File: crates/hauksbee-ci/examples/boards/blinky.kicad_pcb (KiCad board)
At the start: 2 copper layers, 5 parts, among them U1 ATmega328P

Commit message: Add an MCP1702-3302 SOT-23A card and name the DIP-28 package in ATmega328P fixtures
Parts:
- U1: footprint Package_QFP:TQFP-32_7x7mm_P0.8mm -> Package_DIP:DIP-28_W7.62mm
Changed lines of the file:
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@@
-(kicad_pcb(version 20171130)(generator "pcbnew")(general(thickness 1.6))(paper "A4")(layers(0 "F.Cu"signal)(31 "B.Cu"signal)(36 "B.SilkS"user)(37 "F.SilkS"user)(38 "B.Mask"user)(39 "F.Mask"user)(44 "Edge.Cuts"user)(48 "B.Fab"user)(49 "F.Fab"user))(setup(pad_to_mask_clearance 0))(net 0 "")(net 1 "+5V")(net 2 "GND")(net 3 "D13")(net 4 "ADC0")(net 5 "LED_A")(footprint "Resistor_THT:R_Axial_DIN0207_L6.3mm_D2.5mm"(layer "F.Cu")(at -7.198 -6.605 0)(property "Reference""R2")(property "Value""10k")(pad 1 thru_hole circle(at 0 0 0)(size 1 1)(layers "F.Cu")(net 1 "+5V"))(pad 2 thru_hole circle(at 2 0 0)(size 1 1)(layers "F.Cu")(net 4 "ADC0")))(footprint "Resistor_THT:R_Axial_DIN0207_L6.3mm_D2.5mm"(layer "F.Cu")(at 5.69 -0.389 0)(property "Reference""R3")(property "Value""10k")(pad 1 thru_hole circle(at 0 0 0)(size 1 1)(layers "F.Cu")(net 4 "ADC0"))(pad 2 thru_hole circle(at 2 0 0)(size 1 1)(layers "F.Cu")(net 2 "GND")))(footprint "LED_THT:LED_D5.0mm"(layer "F.Cu")(at 4.988 7.204 0)(property "Reference""D1")(property "Value""RED_LED")(pad A thru_hole circle(at 0 0 0)(size 1 1)(layers "F.Cu")(net 5 "LED_A"))(pad K thru_hole circle(at 2 0 0)(size 1 1)(layers "F.Cu")(net 2 "GND")))(footprint "Package_QFP:TQFP-32_7x7mm_P0.8mm"(layer "F.Cu")(at -4.056 2.913 0)(property "Reference""U1")(property "Value""ATmega328P")(pad 7 smd rect(at -3 0 0)(size 0.6 0.6)(layers "F.Cu")(net 1 "+5V"))(pad 8 smd rect(at -3 1 0)(size 0.6 0.6)(layers "F.Cu")(net 2 "GND"))(pad 19 smd rect(at 3 0 0)(size 0.6 0.6)(layers "F.Cu")(net 3 "D13"))(pad 20 smd rect(at 3 1 0)(size 0.6 0.6)(layers "F.Cu")(net 1 "+5V"))(pad 22 smd rect(at 3 2 0)(size 0.6 0.6)(layers "F.Cu")(net 2 "GND"))(pad 23 smd rect(at 3 3 0)(size 0.6 0.6)(layers "F.Cu")(net 4 "ADC0")))(footprint "Resistor_THT:R_Axial_DIN0207_L6.3mm_D2.5mm"(layer "F.Cu")(at 0.805 -6.076 0)(property "Reference""R1")(property "Value""330")(pad 1 thru_hole circle(at 0 0 0)(size 1 1)(layers "F.Cu")(net 3 "D13"))(pad 2 thru_hole circle(at 2 0 0)(size 1 1)(layers "F.Cu")(net 5 "LED_A")))(segment(start -7.056 2.913)(end -7.056 2.08783)(width 0.25)(layer "F.Cu")(net 1))(segment(start -7.056 2.08783)(end -7.198 1.94583)(width 0.25)(layer "F.Cu")(net 1))(segment(start -7.198 1.94583)(end -7.198 -6.605)(width 0.25)(layer "F.Cu")(net 1))(segment(start -1.056 3.913)(end -3.04992 3.913)(width 0.25)(layer "F.Cu")(net 1))(segment(start -3.04992 3.913)(end -4.04992 2.913)(width 0.25)(layer "F.Cu")(net 1))(segment(start -4.04992 2.913)(end -7.056 2.913)(width 0.25)(layer "F.Cu")(net 1))(segment(start 5.69 -0.389)(end 1.805 -4.274)(width 0.25)(layer "F.Cu")(net 4))(segment(start 1.805 -4.274)(end 1.805 -6.24772)(width 0.25)(layer "F.Cu")(net 4))(segment(start 1.805 -6.24772)(end 1.14557 -6.90715)(width 0.25)(layer "F.Cu")(net 4))(segment(start 1.14557 -6.90715)(end -4.89585 -6.90715)(width 0.25)(layer "F.Cu")(net 4))(segment(start -4.89585 -6.90715)(end -5.198 -6.605)(width 0.25)(layer "F.Cu")(net 4))(segment(start -1.056 5.913)(end -0.23083 5.913)(width 0.25)(layer "F.Cu")(net 4))(segment(start -0.23083 5.913)(end -0.23083 5.53183)(width 0.25)(layer "F.Cu")(net 4))(segment(start -0.23083 5.53183)(end 5.69 -0.389)(width 0.25)(layer "F.Cu")(net 4))(segment(start 0.805 -6.076)(end -1.056 -4.215)(width 0.25)(layer "F.Cu")(net 3))(segment(start -1.056 -4.215)(end -1.056 2.913)(width 0.25)(layer "F.Cu")(net 3))(segment(start 6.988 7.204)(end 7.69 6.502)(width 0.25)(layer "B.Cu")(net 2))(segment(start 7.69 6.502)(end 7.69 -0.389)(width 0.25)(layer "B.Cu")(net 2))(segment(start -1.886 4.913)(end -5.23083 4.913)(width 0.25)(layer "F.Cu")(net 2))(segment(start -5.23083 4.913)(end -6.23083 3.913)(width 0.25)(layer "F.Cu")(net 2))(segment(start -1.056 4.913)(end -1.886 4.913)(width 0.25)(layer "F.Cu")(net 2))(segment(start -1.886 4.913)(end -1.886 6.54883)(width 0.25)(layer "F.Cu")(net 2))(segment(start -1.886 6.54883)(end -0.40545 8.02938)(width 0.25)(layer "F.Cu")(net 2))(segment(start -0.40545 8.02938)(end 6.16262 8.02938)(width 0.25)(layer "F.Cu")(net 2))(segment(start 6.16262 8.02938)(end 6.988 7.204)(width 0.25)(layer "F.Cu")(net 2))(segment(start -7.056 3.913)(end -6.23083 3.913)(width 0.25)(layer "F.Cu")(net 2))(segment(start 2.805 -6.076)(end 2.805 5.021)(width 0.25)(layer "B.Cu")(net 5))(segment(start 2.805 5.021)(end 4.988 7.204)(width 0.25)(layer "B.Cu")(net 5)))
+(kicad_pcb(version 20171130)(generator "pcbnew")(general(thickness 1.6))(paper "A4")(layers(0 "F.Cu"signal)(31 "B.Cu"signal)(36 "B.SilkS"user)(37 "F.SilkS"user)(38 "B.Mask"user)(39 "F.Mask"user)(44 "Edge.Cuts"user)(48 "B.Fab"user)(49 "F.Fab"user))(setup(pad_to_mask_clearance 0))(net 0 "")(net 1 "+5V")(net 2 "GND")(net 3 "D13")(net 4 "ADC0")(net 5 "LED_A")(footprint "Resistor_THT:R_Axial_DIN0207_L6.3mm_D2.5mm"(layer "F.Cu")(at -7.198 -6.605 0)(property "Reference""R2")(property "Value""10k")(pad 1 thru_hole circle(at 0 0 0)(size 1 1)(layers "F.Cu")(net 1 "+5V"))(pad 2 thru_hole circle(at 2 0 0)(size 1 1)(layers "F.Cu")(net 4 "ADC0")))(footprint "Resistor_THT:R_Axial_DIN0207_L6.3mm_D2.5mm"(layer "F.Cu")(at 5.69 -0.389 0)(property "Reference""R3")(property "Value""10k")(pad 1 thru_hole circle(at 0 0 0)(size 1 1)(layers "F.Cu")(net 4 "ADC0"))(pad 2 thru_hole circle(at 2 0 0)(size 1 1)(layers "F.Cu")(net 2 "GND")))(footprint "LED_THT:LED_D5.0mm"(layer "F.Cu")(at 4.988 7.204 0)(property "Reference""D1")(property "Value""RED_LED")(pad A thru_hole circle(at 0 0 0)(size 1 1)(layers "F.Cu")(net 5 "LED_A"))(pad K thru_hole circle(at 2 0 0)(size 1 1)(layers "F.Cu")(net 2 "GND")))(footprint "Package_DIP:DIP-28_W7.62mm"(layer "F.Cu")(at -4.056 2.913 0)(property "Reference""U1")(property "Value""ATmega328P")(pad 7 smd rect(at -3 0 0)(size 0.6 0.6)(layers "F.Cu")(net 1 "+5V"))(pad 8 smd rect(at -3 1 0)(size 0.6 0.6)(layers "F.Cu")(net 2 "GND"))(pad 19 smd rect(at 3 0 0)(size 0.6 0.6)(layers "F.Cu")(net 3 "D13"))(pad 20 smd rect(at 3 1 0)(size 0.6 0.6)(layers "F.Cu")(net 1 "+5V"))(pad 22 smd rect(at 3 2 0)(size 0.6 0.6)(layers "F.Cu")(net 2 "GND"))(pad 23 smd rect(at 3 3 0)(size 0.6 0.6)(layers "F.Cu")(net 4 "ADC0")))(footprint "Resistor_THT:R_Axial_DIN0207_L6.3mm_D2.5mm"(layer "F.Cu")(at 0.805 -6.076 0)(property "Reference""R1")(property "Value""330")(pad 1 thru_hole circle(at 0 0 0)(size 1 1)(layers "F.Cu")(net 3 "D13"))(pad 2 thru_hole circle(at 2 0 0)(size 1 1)(layers "F.Cu")(net 5 "LED_A")))(segment(start -7.056 2.913)(end -7.056 2.08783)(width 0.25)(layer "F.Cu")(net 1))(segment(start -7.056 2.08783)(end -7.198 1.94583)(width 0.25)(layer "F.Cu")(net 1))(segment(start -7.198 1.94583)(end -7.198 -6.605)(width 0.25)(layer "F.Cu")(net 1))(segment(start -1.056 3.913)(end -3.04992 3.913)(width 0.25)(layer "F.Cu")(net 1))(segment(start -3.04992 3.913)(end -4.04992 2.913)(width 0.25)(layer "F.Cu")(net 1))(segment(start -4.04992 2.913)(end -7.056 2.913)(width 0.25)(layer "F.Cu")(net 1))(segment(start 5.69 -0.389)(end 1.805 -4.274)(width 0.25)(layer "F.Cu")(net 4))(segment(start 1.805 -4.274)(end 1.805 -6.24772)(width 0.25)(layer "F.Cu")(net 4))(segment(start 1.805 -6.24772)(end 1.14557 -6.90715)(width 0.25)(layer "F.Cu")(net 4))(segment(start 1.14557 -6.90715)(end -4.89585 -6.90715)(width 0.25)(layer "F.Cu")(net 4))(segment(start -4.89585 -6.90715)(end -5.198 -6.605)(width 0.25)(layer "F.Cu")(net 4))(segment(start -1.056 5.913)(end -0.23083 5.913)(width 0.25)(layer "F.Cu")(net 4))(segment(start -0.23083 5.913)(end -0.23083 5.53183)(width 0.25)(layer "F.Cu")(net 4))(segment(start -0.23083 5.53183)(end 5.69 -0.389)(width 0.25)(layer "F.Cu")(net 4))(segment(start 0.805 -6.076)(end -1.056 -4.215)(width 0.25)(layer "F.Cu")(net 3))(segment(start -1.056 -4.215)(end -1.056 2.913)(width 0.25)(layer "F.Cu")(net 3))(segment(start 6.988 7.204)(end 7.69 6.502)(width 0.25)(layer "B.Cu")(net 2))(segment(start 7.69 6.502)(end 7.69 -0.389)(width 0.25)(layer "B.Cu")(net 2))(segment(start -1.886 4.913)(end -5.23083 4.913)(width 0.25)(layer "F.Cu")(net 2))(segment(start -5.23083 4.913)(end -6.23083 3.913)(width 0.25)(layer "F.Cu")(net 2))(segment(start -1.056 4.913)(end -1.886 4.913)(width 0.25)(layer "F.Cu")(net 2))(segment(start -1.886 4.913)(end -1.886 6.54883)(width 0.25)(layer "F.Cu")(net 2))(segment(start -1.886 6.54883)(end -0.40545 8.02938)(width 0.25)(layer "F.Cu")(net 2))(segment(start -0.40545 8.02938)(end 6.16262 8.02938)(width 0.25)(layer "F.Cu")(net 2))(segment(start 6.16262 8.02938)(end 6.988 7.204)(width 0.25)(layer "F.Cu")(net 2))(segment(start -7.056 3.913)(end -6.23083 3.913)(width 0.25)(layer "F.Cu")(net 2))(segment(start 2.805 -6.076)(end 2.805 5.021)(width 0.25)(layer "B.Cu")(net 5))(segment(start 2.805 5.021)(end 4.988 7.204)(width 0.25)(layer "B.Cu")(net 5)))

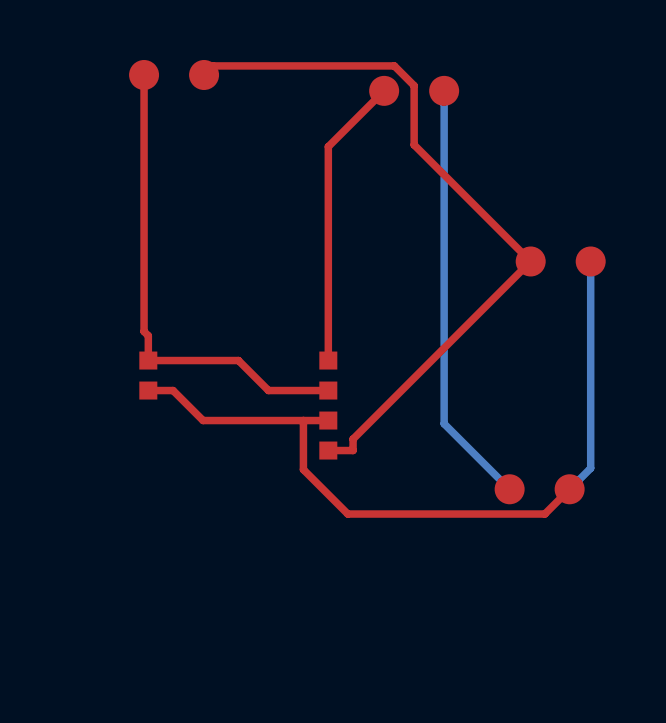
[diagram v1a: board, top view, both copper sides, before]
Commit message: Guessed AVR clocks ride the verdict as their own conditions; fixture boards state their 16 MHz crystal
A guessed core clock is carried as a CiResult verdict condition (not mislabelled
as a partial member sweep). The demo and AT28 fixtures run firmware built for
16 MHz on a bare ATmega328P, so their boards now carry the 16 MHz crystal across
XTAL1/XTAL2 instead of relying on a hard-coded default. Classify backend_id.rs
in the doc-coverage inventory.

Signed-off-by: ETM-Code <158038827+ETM-Code@users.noreply.github.com>
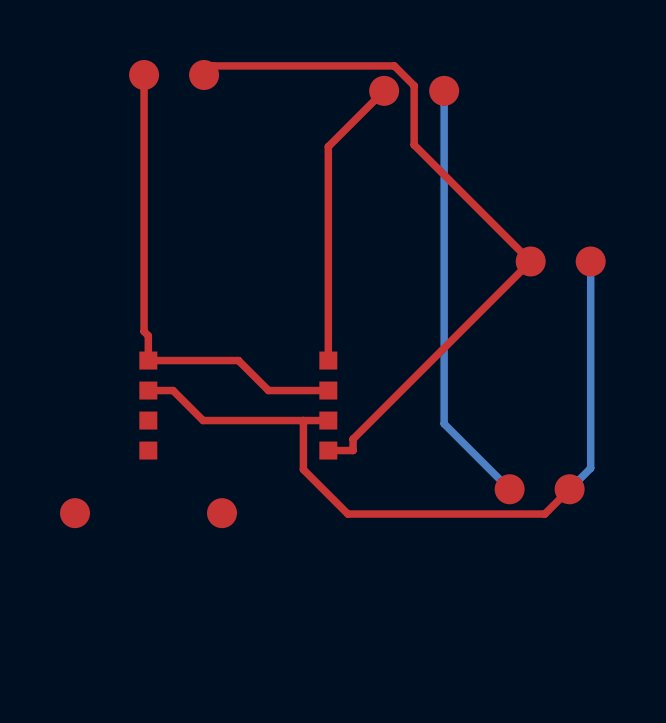
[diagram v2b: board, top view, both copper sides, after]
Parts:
- added Y1: 16MHz, Crystal:Crystal_HC49-4H_Vertical, F.Cu at (-9.50, 8.00)
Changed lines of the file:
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@@
-(kicad_pcb(version 20171130)(generator "pcbnew")(general(thickness 1.6))(paper "A4")(layers(0 "F.Cu"signal)(31 "B.Cu"signal)(36 "B.SilkS"user)(37 "F.SilkS"user)(38 "B.Mask"user)(39 "F.Mask"user)(44 "Edge.Cuts"user)(48 "B.Fab"user)(49 "F.Fab"user))(setup(pad_to_mask_clearance 0))(net 0 "")(net 1 "+5V")(net 2 "GND")(net 3 "D13")(net 4 "ADC0")(net 5 "LED_A")(footprint "Resistor_THT:R_Axial_DIN0207_L6.3mm_D2.5mm"(layer "F.Cu")(at -7.198 -6.605 0)(property "Reference""R2")(property "Value""10k")(pad 1 thru_hole circle(at 0 0 0)(size 1 1)(layers "F.Cu")(net 1 "+5V"))(pad 2 thru_hole circle(at 2 0 0)(size 1 1)(layers "F.Cu")(net 4 "ADC0")))(footprint "Resistor_THT:R_Axial_DIN0207_L6.3mm_D2.5mm"(layer "F.Cu")(at 5.69 -0.389 0)(property "Reference""R3")(property "Value""10k")(pad 1 thru_hole circle(at 0 0 0)(size 1 1)(layers "F.Cu")(net 4 "ADC0"))(pad 2 thru_hole circle(at 2 0 0)(size 1 1)(layers "F.Cu")(net 2 "GND")))(footprint "LED_THT:LED_D5.0mm"(layer "F.Cu")(at 4.988 7.204 0)(property "Reference""D1")(property "Value""RED_LED")(pad A thru_hole circle(at 0 0 0)(size 1 1)(layers "F.Cu")(net 5 "LED_A"))(pad K thru_hole circle(at 2 0 0)(size 1 1)(layers "F.Cu")(net 2 "GND")))(footprint "Package_DIP:DIP-28_W7.62mm"(layer "F.Cu")(at -4.056 2.913 0)(property "Reference""U1")(property "Value""ATmega328P")(pad 7 smd rect(at -3 0 0)(size 0.6 0.6)(layers "F.Cu")(net 1 "+5V"))(pad 8 smd rect(at -3 1 0)(size 0.6 0.6)(layers "F.Cu")(net 2 "GND"))(pad 19 smd rect(at 3 0 0)(size 0.6 0.6)(layers "F.Cu")(net 3 "D13"))(pad 20 smd rect(at 3 1 0)(size 0.6 0.6)(layers "F.Cu")(net 1 "+5V"))(pad 22 smd rect(at 3 2 0)(size 0.6 0.6)(layers "F.Cu")(net 2 "GND"))(pad 23 smd rect(at 3 3 0)(size 0.6 0.6)(layers "F.Cu")(net 4 "ADC0")))(footprint "Resistor_THT:R_Axial_DIN0207_L6.3mm_D2.5mm"(layer "F.Cu")(at 0.805 -6.076 0)(property "Reference""R1")(property "Value""330")(pad 1 thru_hole circle(at 0 0 0)(size 1 1)(layers "F.Cu")(net 3 "D13"))(pad 2 thru_hole circle(at 2 0 0)(size 1 1)(layers "F.Cu")(net 5 "LED_A")))(segment(start -7.056 2.913)(end -7.056 2.08783)(width 0.25)(layer "F.Cu")(net 1))(segment(start -7.056 2.08783)(end -7.198 1.94583)(width 0.25)(layer "F.Cu")(net 1))(segment(start -7.198 1.94583)(end -7.198 -6.605)(width 0.25)(layer "F.Cu")(net 1))(segment(start -1.056 3.913)(end -3.04992 3.913)(width 0.25)(layer "F.Cu")(net 1))(segment(start -3.04992 3.913)(end -4.04992 2.913)(width 0.25)(layer "F.Cu")(net 1))(segment(start -4.04992 2.913)(end -7.056 2.913)(width 0.25)(layer "F.Cu")(net 1))(segment(start 5.69 -0.389)(end 1.805 -4.274)(width 0.25)(layer "F.Cu")(net 4))(segment(start 1.805 -4.274)(end 1.805 -6.24772)(width 0.25)(layer "F.Cu")(net 4))(segment(start 1.805 -6.24772)(end 1.14557 -6.90715)(width 0.25)(layer "F.Cu")(net 4))(segment(start 1.14557 -6.90715)(end -4.89585 -6.90715)(width 0.25)(layer "F.Cu")(net 4))(segment(start -4.89585 -6.90715)(end -5.198 -6.605)(width 0.25)(layer "F.Cu")(net 4))(segment(start -1.056 5.913)(end -0.23083 5.913)(width 0.25)(layer "F.Cu")(net 4))(segment(start -0.23083 5.913)(end -0.23083 5.53183)(width 0.25)(layer "F.Cu")(net 4))(segment(start -0.23083 5.53183)(end 5.69 -0.389)(width 0.25)(layer "F.Cu")(net 4))(segment(start 0.805 -6.076)(end -1.056 -4.215)(width 0.25)(layer "F.Cu")(net 3))(segment(start -1.056 -4.215)(end -1.056 2.913)(width 0.25)(layer "F.Cu")(net 3))(segment(start 6.988 7.204)(end 7.69 6.502)(width 0.25)(layer "B.Cu")(net 2))(segment(start 7.69 6.502)(end 7.69 -0.389)(width 0.25)(layer "B.Cu")(net 2))(segment(start -1.886 4.913)(end -5.23083 4.913)(width 0.25)(layer "F.Cu")(net 2))(segment(start -5.23083 4.913)(end -6.23083 3.913)(width 0.25)(layer "F.Cu")(net 2))(segment(start -1.056 4.913)(end -1.886 4.913)(width 0.25)(layer "F.Cu")(net 2))(segment(start -1.886 4.913)(end -1.886 6.54883)(width 0.25)(layer "F.Cu")(net 2))(segment(start -1.886 6.54883)(end -0.40545 8.02938)(width 0.25)(layer "F.Cu")(net 2))(segment(start -0.40545 8.02938)(end 6.16262 8.02938)(width 0.25)(layer "F.Cu")(net 2))(segment(start 6.16262 8.02938)(end 6.988 7.204)(width 0.25)(layer "F.Cu")(net 2))(segment(start -7.056 3.913)(end -6.23083 3.913)(width 0.25)(layer "F.Cu")(net 2))(segment(start 2.805 -6.076)(end 2.805 5.021)(width 0.25)(layer "B.Cu")(net 5))(segment(start 2.805 5.021)(end 4.988 7.204)(width 0.25)(layer "B.Cu")(net 5)))
+(kicad_pcb(version 20171130)(generator "pcbnew")(general(thickness 1.6))(paper "A4")(layers(0 "F.Cu"signal)(31 "B.Cu"signal)(36 "B.SilkS"user)(37 "F.SilkS"user)(38 "B.Mask"user)(39 "F.Mask"user)(44 "Edge.Cuts"user)(48 "B.Fab"user)(49 "F.Fab"user))(setup(pad_to_mask_clearance 0))(net 0 "")(net 1 "+5V")(net 2 "GND")(net 3 "D13")(net 4 "ADC0")(net 5 "LED_A")(net 6 "XTAL1")(net 7 "XTAL2")(footprint "Resistor_THT:R_Axial_DIN0207_L6.3mm_D2.5mm"(layer "F.Cu")(at -7.198 -6.605 0)(property "Reference""R2")(property "Value""10k")(pad 1 thru_hole circle(at 0 0 0)(size 1 1)(layers "F.Cu")(net 1 "+5V"))(pad 2 thru_hole circle(at 2 0 0)(size 1 1)(layers "F.Cu")(net 4 "ADC0")))(footprint "Resistor_THT:R_Axial_DIN0207_L6.3mm_D2.5mm"(layer "F.Cu")(at 5.69 -0.389 0)(property "Reference""R3")(property "Value""10k")(pad 1 thru_hole circle(at 0 0 0)(size 1 1)(layers "F.Cu")(net 4 "ADC0"))(pad 2 thru_hole circle(at 2 0 0)(size 1 1)(layers "F.Cu")(net 2 "GND")))(footprint "LED_THT:LED_D5.0mm"(layer "F.Cu")(at 4.988 7.204 0)(property "Reference""D1")(property "Value""RED_LED")(pad A thru_hole circle(at 0 0 0)(size 1 1)(layers "F.Cu")(net 5 "LED_A"))(pad K thru_hole circle(at 2 0 0)(size 1 1)(layers "F.Cu")(net 2 "GND")))(footprint "Package_DIP:DIP-28_W7.62mm"(layer "F.Cu")(at -4.056 2.913 0)(property "Reference""U1")(property "Value""ATmega328P")(pad 7 smd rect(at -3 0 0)(size 0.6 0.6)(layers "F.Cu")(net 1 "+5V"))(pad 8 smd rect(at -3 1 0)(size 0.6 0.6)(layers "F.Cu")(net 2 "GND"))(pad 9 smd rect(at -3 2 0)(size 0.6 0.6)(layers "F.Cu")(net 6 "XTAL1"))(pad 10 smd rect(at -3 3 0)(size 0.6 0.6)(layers "F.Cu")(net 7 "XTAL2"))(pad 19 smd rect(at 3 0 0)(size 0.6 0.6)(layers "F.Cu")(net 3 "D13"))(pad 20 smd rect(at 3 1 0)(size 0.6 0.6)(layers "F.Cu")(net 1 "+5V"))(pad 22 smd rect(at 3 2 0)(size 0.6 0.6)(layers "F.Cu")(net 2 "GND"))(pad 23 smd rect(at 3 3 0)(size 0.6 0.6)(layers "F.Cu")(net 4 "ADC0")))(footprint "Crystal:Crystal_HC49-4H_Vertical"(layer "F.Cu")(at -9.5 8 0)(property "Reference""Y1")(property "Value""16MHz")(pad 1 thru_hole circle(at 0 0 0)(size 1 1)(layers "F.Cu")(net 6 "XTAL1"))(pad 2 thru_hole circle(at 4.9 0 0)(size 1 1)(layers "F.Cu")(net 7 "XTAL2")))(footprint "Resistor_THT:R_Axial_DIN0207_L6.3mm_D2.5mm"(layer "F.Cu")(at 0.805 -6.076 0)(property "Reference""R1")(property "Value""330")(pad 1 thru_hole circle(at 0 0 0)(size 1 1)(layers "F.Cu")(net 3 "D13"))(pad 2 thru_hole circle(at 2 0 0)(size 1 1)(layers "F.Cu")(net 5 "LED_A")))(segment(start -7.056 2.913)(end -7.056 2.08783)(width 0.25)(layer "F.Cu")(net 1))(segment(start -7.056 2.08783)(end -7.198 1.94583)(width 0.25)(layer "F.Cu")(net 1))(segment(start -7.198 1.94583)(end -7.198 -6.605)(width 0.25)(layer "F.Cu")(net 1))(segment(start -1.056 3.913)(end -3.04992 3.913)(width 0.25)(layer "F.Cu")(net 1))(segment(start -3.04992 3.913)(end -4.04992 2.913)(width 0.25)(layer "F.Cu")(net 1))(segment(start -4.04992 2.913)(end -7.056 2.913)(width 0.25)(layer "F.Cu")(net 1))(segment(start 5.69 -0.389)(end 1.805 -4.274)(width 0.25)(layer "F.Cu")(net 4))(segment(start 1.805 -4.274)(end 1.805 -6.24772)(width 0.25)(layer "F.Cu")(net 4))(segment(start 1.805 -6.24772)(end 1.14557 -6.90715)(width 0.25)(layer "F.Cu")(net 4))(segment(start 1.14557 -6.90715)(end -4.89585 -6.90715)(width 0.25)(layer "F.Cu")(net 4))(segment(start -4.89585 -6.90715)(end -5.198 -6.605)(width 0.25)(layer "F.Cu")(net 4))(segment(start -1.056 5.913)(end -0.23083 5.913)(width 0.25)(layer "F.Cu")(net 4))(segment(start -0.23083 5.913)(end -0.23083 5.53183)(width 0.25)(layer "F.Cu")(net 4))(segment(start -0.23083 5.53183)(end 5.69 -0.389)(width 0.25)(layer "F.Cu")(net 4))(segment(start 0.805 -6.076)(end -1.056 -4.215)(width 0.25)(layer "F.Cu")(net 3))(segment(start -1.056 -4.215)(end -1.056 2.913)(width 0.25)(layer "F.Cu")(net 3))(segment(start 6.988 7.204)(end 7.69 6.502)(width 0.25)(layer "B.Cu")(net 2))(segment(start 7.69 6.502)(end 7.69 -0.389)(width 0.25)(layer "B.Cu")(net 2))(segment(start -1.886 4.913)(end -5.23083 4.913)(width 0.25)(layer "F.Cu")(net 2))(segment(start -5.23083 4.913)(end -6.23083 3.913)(width 0.25)(layer "F.Cu")(net 2))(segment(start -1.056 4.913)(end -1.886 4.913)(width 0.25)(layer "F.Cu")(net 2))(segment(start -1.886 4.913)(end -1.886 6.54883)(width 0.25)(layer "F.Cu")(net 2))(segment(start -1.886 6.54883)(end -0.40545 8.02938)(width 0.25)(layer "F.Cu")(net 2))(segment(start -0.40545 8.02938)(end 6.16262 8.02938)(width 0.25)(layer "F.Cu")(net 2))(segment(start 6.16262 8.02938)(end 6.988 7.204)(width 0.25)(layer "F.Cu")(net 2))(segment(start -7.056 3.913)(end -6.23083 3.913)(width 0.25)(layer "F.Cu")(net 2))(segment(start 2.805 -6.076)(end 2.805 5.021)(width 0.25)(layer "B.Cu")(net 5))(segment(start 2.805 5.021)(end 4.988 7.204)(width 0.25)(layer "B.Cu")(net 5)))
